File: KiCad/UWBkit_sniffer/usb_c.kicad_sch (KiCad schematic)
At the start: 9 parts, among them J6 USB_C_Receptacle_USB2.0_14P, U5 IP4234CZ6

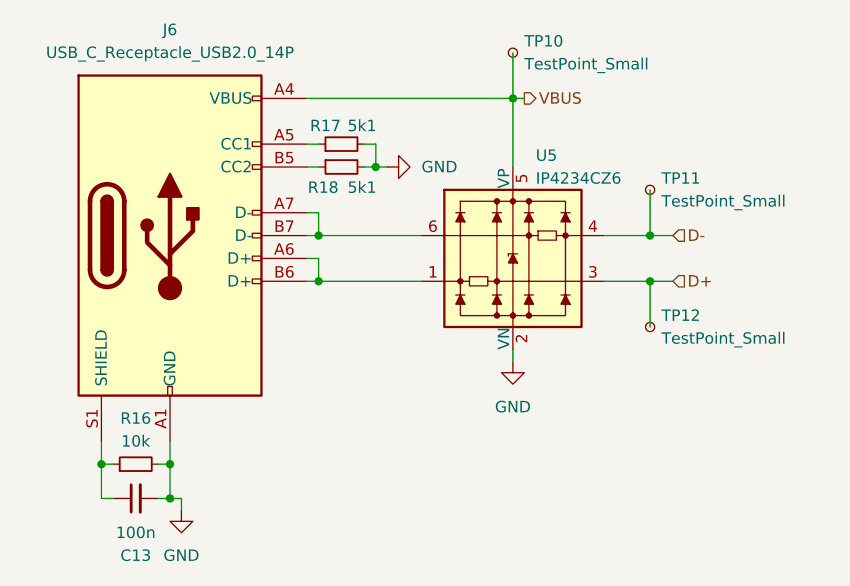
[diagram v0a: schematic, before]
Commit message: United 5V rails, modified layout of connectors
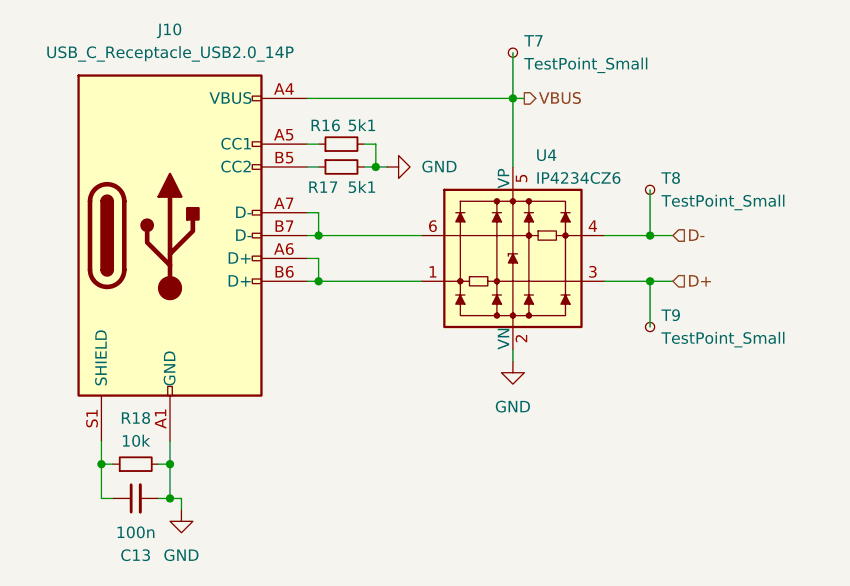
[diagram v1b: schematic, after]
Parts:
- renumbered J6 to J10, R17 to R16, R18 to R17, R16 to R18, TP10 to T7, TP11 to T8, TP12 to T9, U5 to U4
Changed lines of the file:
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@@
 		(dnp no)
 		(fields_autoplaced yes)
-		(property "Reference" "R16"
+		(property "Reference" "R18"
 			(at 127 110.49 90)
 			(effects
@@
 			(project "UWBkit_sniffer"
 				(path "/7666dc1a-7b28-48ea-a5e3-eea89f700cea/c350af74-d5e5-4753-8aec-daa1a6b2f7b0"
-					(reference "R19")
-					(unit 1)
-				)
-				(path "/7666dc1a-7b28-48ea-a5e3-eea89f700cea/e0202866-7f47-40a7-b0f0-606576789748"
-					(reference "R16")
+					(reference "R21")
+					(unit 1)
+				)
+				(path "/7666dc1a-7b28-48ea-a5e3-eea89f700cea/e0202866-7f47-40a7-b0f0-606576789748"
+					(reference "R18")
 					(unit 1)
 				)
@@
 		(dnp no)
 		(fields_autoplaced yes)
-		(property "Reference" "#PWR027"
+		(property "Reference" "#PWR060"
 			(at 168.91 110.49 0)
 			(effects
@@
 			(project "UWBkit_sniffer"
 				(path "/7666dc1a-7b28-48ea-a5e3-eea89f700cea/c350af74-d5e5-4753-8aec-daa1a6b2f7b0"
-					(reference "#PWR031")
-					(unit 1)
-				)
-				(path "/7666dc1a-7b28-48ea-a5e3-eea89f700cea/e0202866-7f47-40a7-b0f0-606576789748"
-					(reference "#PWR027")
+					(reference "#PWR063")
+					(unit 1)
+				)
+				(path "/7666dc1a-7b28-48ea-a5e3-eea89f700cea/e0202866-7f47-40a7-b0f0-606576789748"
+					(reference "#PWR060")
 					(unit 1)
 				)
@@
 		(on_board yes)
 		(dnp no)
-		(property "Reference" "R17"
+		(property "Reference" "R16"
 			(at 148.082 77.978 90)
 			(effects
@@
 			(project "UWBkit_sniffer"
 				(path "/7666dc1a-7b28-48ea-a5e3-eea89f700cea/c350af74-d5e5-4753-8aec-daa1a6b2f7b0"
-					(reference "R20")
-					(unit 1)
-				)
-				(path "/7666dc1a-7b28-48ea-a5e3-eea89f700cea/e0202866-7f47-40a7-b0f0-606576789748"
-					(reference "R17")
+					(reference "R19")
+					(unit 1)
+				)
+				(path "/7666dc1a-7b28-48ea-a5e3-eea89f700cea/e0202866-7f47-40a7-b0f0-606576789748"
+					(reference "R16")
 					(unit 1)
 				)
@@
 		(on_board yes)
 		(dnp no)
-		(property "Reference" "TP11"
+		(property "Reference" "T8"
 			(at 185.42 83.8199 0)
 			(effects
@@
 			(project "UWBkit_sniffer"
 				(path "/7666dc1a-7b28-48ea-a5e3-eea89f700cea/c350af74-d5e5-4753-8aec-daa1a6b2f7b0"
-					(reference "TP14")
-					(unit 1)
-				)
-				(path "/7666dc1a-7b28-48ea-a5e3-eea89f700cea/e0202866-7f47-40a7-b0f0-606576789748"
-					(reference "TP11")
+					(reference "T11")
+					(unit 1)
+				)
+				(path "/7666dc1a-7b28-48ea-a5e3-eea89f700cea/e0202866-7f47-40a7-b0f0-606576789748"
+					(reference "T8")
 					(unit 1)
 				)
@@
 		(on_board yes)
 		(dnp no)
-		(property "Reference" "J6"
+		(property "Reference" "J10"
 			(at 130.81 67.31 0)
 			(effects
@@
 			(project "UWBkit_sniffer"
 				(path "/7666dc1a-7b28-48ea-a5e3-eea89f700cea/c350af74-d5e5-4753-8aec-daa1a6b2f7b0"
-					(reference "J7")
-					(unit 1)
-				)
-				(path "/7666dc1a-7b28-48ea-a5e3-eea89f700cea/e0202866-7f47-40a7-b0f0-606576789748"
-					(reference "J6")
+					(reference "J11")
+					(unit 1)
+				)
+				(path "/7666dc1a-7b28-48ea-a5e3-eea89f700cea/e0202866-7f47-40a7-b0f0-606576789748"
+					(reference "J10")
 					(unit 1)
 				)
@@
 		(on_board yes)
 		(dnp no)
-		(property "Reference" "U5"
+		(property "Reference" "U4"
 			(at 171.45 81.28 0)
 			(effects
@@
 			(project "UWBkit_sniffer"
 				(path "/7666dc1a-7b28-48ea-a5e3-eea89f700cea/c350af74-d5e5-4753-8aec-daa1a6b2f7b0"
-					(reference "U6")
-					(unit 1)
-				)
-				(path "/7666dc1a-7b28-48ea-a5e3-eea89f700cea/e0202866-7f47-40a7-b0f0-606576789748"
 					(reference "U5")
+					(unit 1)
+				)
+				(path "/7666dc1a-7b28-48ea-a5e3-eea89f700cea/e0202866-7f47-40a7-b0f0-606576789748"
+					(reference "U4")
 					(unit 1)
 				)
@@
 		(on_board yes)
 		(dnp no)
-		(property "Reference" "TP12"
+		(property "Reference" "T9"
 			(at 185.42 99.0599 0)
 			(effects
@@
 			(project "UWBkit_sniffer"
 				(path "/7666dc1a-7b28-48ea-a5e3-eea89f700cea/c350af74-d5e5-4753-8aec-daa1a6b2f7b0"
-					(reference "TP15")
-					(unit 1)
-				)
-				(path "/7666dc1a-7b28-48ea-a5e3-eea89f700cea/e0202866-7f47-40a7-b0f0-606576789748"
-					(reference "TP12")
+					(reference "T12")
+					(unit 1)
+				)
+				(path "/7666dc1a-7b28-48ea-a5e3-eea89f700cea/e0202866-7f47-40a7-b0f0-606576789748"
+					(reference "T9")
 					(unit 1)
 				)
@@
 		(dnp no)
 		(fields_autoplaced yes)
-		(property "Reference" "#PWR024"
+		(property "Reference" "#PWR061"
 			(at 132.08 127 0)
 			(effects
@@
 			(project "UWBkit_sniffer"
 				(path "/7666dc1a-7b28-48ea-a5e3-eea89f700cea/c350af74-d5e5-4753-8aec-daa1a6b2f7b0"
-					(reference "#PWR026")
-					(unit 1)
-				)
-				(path "/7666dc1a-7b28-48ea-a5e3-eea89f700cea/e0202866-7f47-40a7-b0f0-606576789748"
-					(reference "#PWR024")
+					(reference "#PWR064")
+					(unit 1)
+				)
+				(path "/7666dc1a-7b28-48ea-a5e3-eea89f700cea/e0202866-7f47-40a7-b0f0-606576789748"
+					(reference "#PWR061")
 					(unit 1)
 				)
@@
 		(on_board yes)
 		(dnp no)
-		(property "Reference" "R18"
+		(property "Reference" "R17"
 			(at 147.828 84.836 90)
 			(effects
@@
 			(project "UWBkit_sniffer"
 				(path "/7666dc1a-7b28-48ea-a5e3-eea89f700cea/c350af74-d5e5-4753-8aec-daa1a6b2f7b0"
-					(reference "R21")
-					(unit 1)
-				)
-				(path "/7666dc1a-7b28-48ea-a5e3-eea89f700cea/e0202866-7f47-40a7-b0f0-606576789748"
-					(reference "R18")
+					(reference "R20")
+					(unit 1)
+				)
+				(path "/7666dc1a-7b28-48ea-a5e3-eea89f700cea/e0202866-7f47-40a7-b0f0-606576789748"
+					(reference "R17")
 					(unit 1)
 				)
@@
 		(on_board yes)
 		(dnp no)
-		(property "Reference" "TP10"
+		(property "Reference" "T7"
 			(at 170.18 68.5799 0)
 			(effects
@@
 			(project "UWBkit_sniffer"
 				(path "/7666dc1a-7b28-48ea-a5e3-eea89f700cea/c350af74-d5e5-4753-8aec-daa1a6b2f7b0"
-					(reference "TP13")
-					(unit 1)
-				)
-				(path "/7666dc1a-7b28-48ea-a5e3-eea89f700cea/e0202866-7f47-40a7-b0f0-606576789748"
-					(reference "TP10")
+					(reference "T10")
+					(unit 1)
+				)
+				(path "/7666dc1a-7b28-48ea-a5e3-eea89f700cea/e0202866-7f47-40a7-b0f0-606576789748"
+					(reference "T7")
 					(unit 1)
 				)
@@
 		(dnp no)
 		(fields_autoplaced yes)
-		(property "Reference" "#PWR025"
+		(property "Reference" "#PWR059"
 			(at 161.29 82.55 0)
 			(effects
@@
 			(project "UWBkit_sniffer"
 				(path "/7666dc1a-7b28-48ea-a5e3-eea89f700cea/c350af74-d5e5-4753-8aec-daa1a6b2f7b0"
-					(reference "#PWR029")
-					(unit 1)
-				)
-				(path "/7666dc1a-7b28-48ea-a5e3-eea89f700cea/e0202866-7f47-40a7-b0f0-606576789748"
-					(reference "#PWR025")
-					(unit 1)
-				)
+					(reference "#PWR062")
+					(unit 1)
+				)
+				(path "/7666dc1a-7b28-48ea-a5e3-eea89f700cea/e0202866-7f47-40a7-b0f0-606576789748"
+					(reference "#PWR059")
+					(unit 1)
+				)

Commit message: Removed UWA.01, added CTS/RTS connections
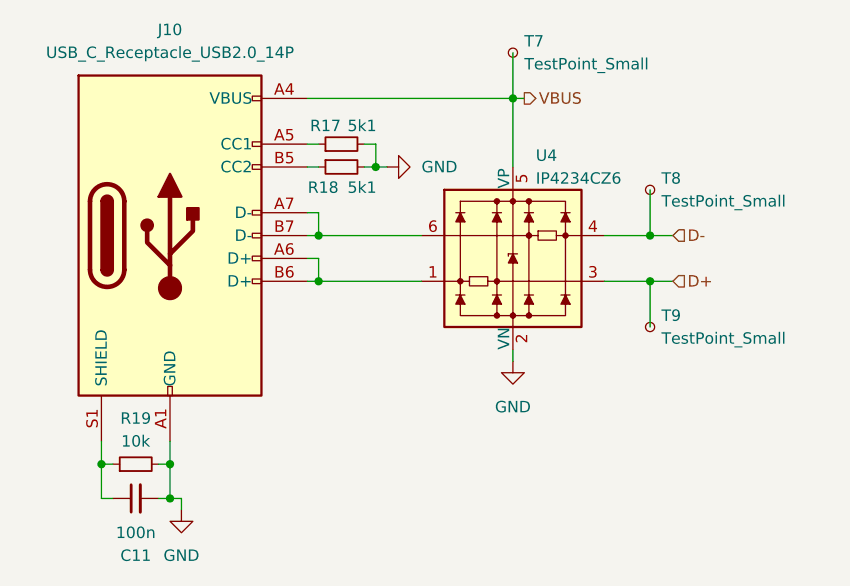
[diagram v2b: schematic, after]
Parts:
- renumbered C13 to C11, R16 to R17, R17 to R18, R18 to R19
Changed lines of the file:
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@@
 		(dnp no)
 		(fields_autoplaced yes)
-		(property "Reference" "R18"
+		(property "Reference" "R19"
 			(at 127 110.49 90)
 			(effects
@@
 			(project "UWBkit_sniffer"
 				(path "/7666dc1a-7b28-48ea-a5e3-eea89f700cea/c350af74-d5e5-4753-8aec-daa1a6b2f7b0"
-					(reference "R21")
-					(unit 1)
-				)
-				(path "/7666dc1a-7b28-48ea-a5e3-eea89f700cea/e0202866-7f47-40a7-b0f0-606576789748"
-					(reference "R18")
+					(reference "R22")
+					(unit 1)
+				)
+				(path "/7666dc1a-7b28-48ea-a5e3-eea89f700cea/e0202866-7f47-40a7-b0f0-606576789748"
+					(reference "R19")
 					(unit 1)
 				)
@@
 		(on_board yes)
 		(dnp no)
-		(property "Reference" "R16"
+		(property "Reference" "R17"
 			(at 148.082 77.978 90)
 			(effects
@@
 			(project "UWBkit_sniffer"
 				(path "/7666dc1a-7b28-48ea-a5e3-eea89f700cea/c350af74-d5e5-4753-8aec-daa1a6b2f7b0"
-					(reference "R19")
-					(unit 1)
-				)
-				(path "/7666dc1a-7b28-48ea-a5e3-eea89f700cea/e0202866-7f47-40a7-b0f0-606576789748"
-					(reference "R16")
+					(reference "R20")
+					(unit 1)
+				)
+				(path "/7666dc1a-7b28-48ea-a5e3-eea89f700cea/e0202866-7f47-40a7-b0f0-606576789748"
+					(reference "R17")
 					(unit 1)
 				)
@@
 		(on_board yes)
 		(dnp no)
-		(property "Reference" "C13"
+		(property "Reference" "C11"
 			(at 127.0063 125.73 90)
 			(effects
@@
 			(project "UWBkit_sniffer"
 				(path "/7666dc1a-7b28-48ea-a5e3-eea89f700cea/c350af74-d5e5-4753-8aec-daa1a6b2f7b0"
-					(reference "C14")
-					(unit 1)
-				)
-				(path "/7666dc1a-7b28-48ea-a5e3-eea89f700cea/e0202866-7f47-40a7-b0f0-606576789748"
-					(reference "C13")
+					(reference "C12")
+					(unit 1)
+				)
+				(path "/7666dc1a-7b28-48ea-a5e3-eea89f700cea/e0202866-7f47-40a7-b0f0-606576789748"
+					(reference "C11")
 					(unit 1)
 				)
@@
 		(on_board yes)
 		(dnp no)
-		(property "Reference" "R17"
+		(property "Reference" "R18"
 			(at 147.828 84.836 90)
 			(effects
@@
 			(project "UWBkit_sniffer"
 				(path "/7666dc1a-7b28-48ea-a5e3-eea89f700cea/c350af74-d5e5-4753-8aec-daa1a6b2f7b0"
-					(reference "R20")
-					(unit 1)
-				)
-				(path "/7666dc1a-7b28-48ea-a5e3-eea89f700cea/e0202866-7f47-40a7-b0f0-606576789748"
-					(reference "R17")
-					(unit 1)
-				)
+					(reference "R21")
+					(unit 1)
+				)
+				(path "/7666dc1a-7b28-48ea-a5e3-eea89f700cea/e0202866-7f47-40a7-b0f0-606576789748"
+					(reference "R18")
+					(unit 1)
+				)

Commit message: Release V1.0
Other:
- title: (none) -> USB Typer C Connector
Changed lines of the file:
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@@
 	(generator_version "9.0")
 	(paper "A4")
+	(title_block
+		(title "USB Typer C Connector")
+		(date "2026-02-24")
+		(rev "1.0")
+	)
 	(junction
 		(at 184.15 95.25)
